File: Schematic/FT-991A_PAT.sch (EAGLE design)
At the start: 38 parts, among them Q1 PE4259, Q2 MC78L09, Q3 DG2001, Q5 NCP553, Q7 J310, Q8 BFR193F, X1 IF_IN, X2 SCP_OUT, X3 SDR_OUT

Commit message: Announcing: Revision U
Featuring:
* A properly matched BFR193F transistor, yielding 7 dB of gain,
  surpassing 2SC5086
* Larger pads for BFR193F
* Few routing improvements, larger wires
* Removed a via near the 3V regulator, didnt help a lot and was
  a short circuit risk.
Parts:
- C11, C12: value 330pF -> 1000pF
- C13: value 0.047µF -> 4.7 nF; device aarf:C-0805 -> aarf:C-1206
- C14: value 15pF -> 47pF
- L1: value 91nH -> 82nH
- R11: value 33kΩ -> 39kΩ
- R13: value 10Ω -> 27Ω
- R14: value 10Ω -> 47Ω
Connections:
- net BIAS renamed ST2OUT
- net IFIN renamed ST1IN
- net N$1 renamed ST2M2
- net N$3 renamed ST2M1
- net N$4 renamed ST2IN
- net N$5 renamed ST1M1
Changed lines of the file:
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@@
 <attribute name="PROJECT_INFO" value="Yaesu FT-991A Panadapter with Signal Control"/>
 <attribute name="PROJECT_NAME" value="FT-991A PAT &amp; SDR"/>
-<attribute name="REVISION_ID" value="T"/>
+<attribute name="REVISION_ID" value="U"/>
 </attributes>
 <variantdefs>
@@
 <part name="Q8" library="aarf" deviceset="BFR193F" device="" value="BFR193F"/>
 <part name="R7" library="aarf" deviceset="R-1206" device="" value="1kΩ"/>
-<part name="C11" library="aarf" deviceset="C-0805" device="" value="330pF"/>
+<part name="C11" library="aarf" deviceset="C-0805" device="" value="1000pF"/>
 <part name="GND11" library="supply1" deviceset="GNDA" device=""/>
 <part name="C2" library="aarf" deviceset="C-1206" device="" value="0.1µF"/>
 <part name="GND10" library="supply1" deviceset="GNDA" device=""/>
 <part name="C3" library="aarf" deviceset="C-1206" device="" value="0.1µF"/>
-<part name="R11" library="aarf" deviceset="R-1206" device="" value="33kΩ"/>
+<part name="R11" library="aarf" deviceset="R-1206" device="" value="39kΩ"/>
 <part name="GND19" library="supply1" deviceset="GNDA" device=""/>
 <part name="GND13" library="supply1" deviceset="GNDA" device=""/>
@@
 <part name="GND2" library="supply1" library_urn="urn:adsk.eagle:library:371" deviceset="GNDA" device=""/>
 <part name="L3" library="aarf" deviceset="FB-0805" device="" value="BLM21"/>
-<part name="C12" library="aarf" deviceset="C-0805" device="" value="330pF"/>
+<part name="C12" library="aarf" deviceset="C-0805" device="" value="1000pF"/>
 <part name="FRAME2" library="frames" library_urn="urn:adsk.eagle:library:229" deviceset="A3L-LOC" device=""/>
 <part name="GND5" library="supply1" library_urn="urn:adsk.eagle:library:371" deviceset="GNDA" device=""/>
@@
 <part name="GND7" library="supply1" deviceset="GNDA" device=""/>
 <part name="GND8" library="supply1" deviceset="GNDA" device=""/>
-<part name="R13" library="aarf" deviceset="R-1206" device="" value="10Ω"/>
+<part name="R13" library="aarf" deviceset="R-1206" device="" value="27Ω"/>
 <part name="R12" library="aarf" deviceset="R-1206" device="" value="100Ω"/>
-<part name="R14" library="aarf" deviceset="R-1206" device="" value="10Ω"/>
-<part name="C13" library="aarf" deviceset="C-0805" device="" value="0.047µF"/>
+<part name="R14" library="aarf" deviceset="R-1206" device="" value="47Ω"/>
+<part name="C13" library="aarf" deviceset="C-1206" device="" value="4.7 nF"/>
 <part name="GND9" library="supply1" deviceset="GNDA" device=""/>
-<part name="L1" library="aarf" deviceset="L-0805" device="" value="91nH">
+<part name="L1" library="aarf" deviceset="L-0805" device="" value="82nH">
 <spice>
 <pinmapping isusermap="yes" isdevicewide="yes">
@@
 <attribute name="SPICEPREFIX" value="L"/>
 </part>
-<part name="C14" library="aarf" deviceset="C-0805" device="" value="15pF"/>
+<part name="C14" library="aarf" deviceset="C-0805" device="" value="47pF"/>
 <part name="GND14" library="supply1" deviceset="GNDA" device=""/>
 </parts>
@@
 </busses>
 <nets>
-<net name="N$4" class="0">
+<net name="ST2IN" class="0">
 <segment>
 <pinref part="C11" gate="G$1" pin="2"/>
@@
 </segment>
 </net>
-<net name="N$5" class="0">
+<net name="ST1M1" class="0">
 <segment>
 <pinref part="R7" gate="G$1" pin="2"/>
@@
 </segment>
 </net>
-<net name="IFIN" class="0">
+<net name="ST1IN" class="0">
 <segment>
 <pinref part="Q1" gate="G$1" pin="RF2"/>
@@
 </segment>
 </net>
-<net name="BIAS" class="0">
+<net name="ST2OUT" class="0">
 <segment>
 <pinref part="R12" gate="G$1" pin="2"/>
@@
 </segment>
 </net>
-<net name="N$3" class="0">
+<net name="ST2M1" class="0">
 <segment>
 <pinref part="R14" gate="G$1" pin="2"/>
@@
 </segment>
 </net>
-<net name="N$1" class="0">
+<net name="ST2M2" class="0">
 <segment>
 <pinref part="C12" gate="G$1" pin="2"/>

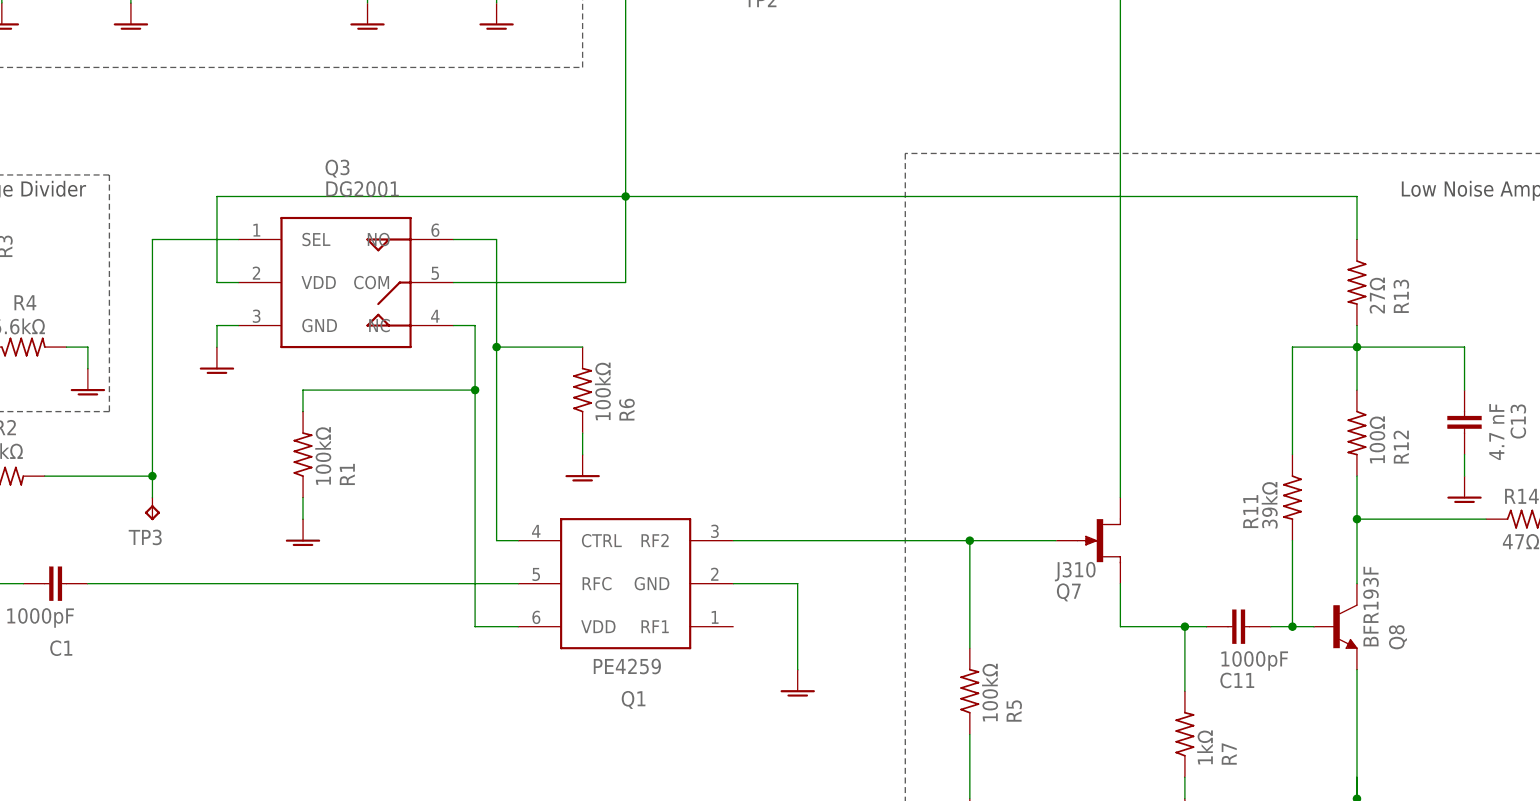
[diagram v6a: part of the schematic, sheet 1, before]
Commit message: Updating Schematic and Board
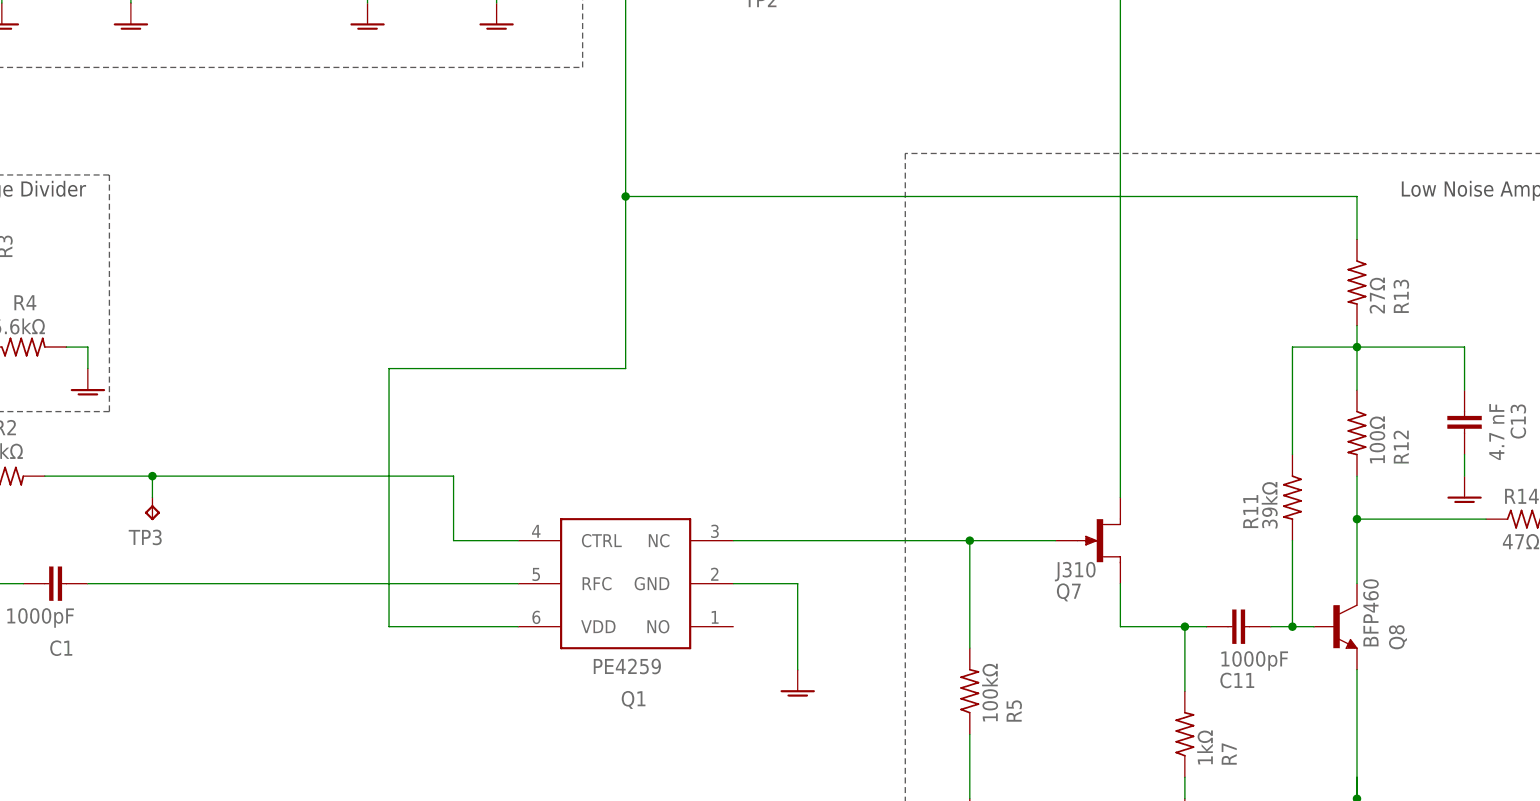
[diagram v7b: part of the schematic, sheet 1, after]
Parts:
- removed Q3: DG2001, aarf:NLAS4599
- removed R1, R6: 100kΩ, aarf:R-1206
- Q8: value BFR193F -> BFP460; device aarf:BFR193F -> aarf:BFP460
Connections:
- removed net NC: Q1.VDD, Q3.NC, R1.2
- removed net NO: Q1.CTRL, Q3.NO, R6.2
- net 3V: now also Q1.VDD; no longer Q3.COM, Q3.VDD
- net GNDA: no longer Q3.GND, R1.1, R6.1
- net N$7: now also Q1.CTRL; no longer Q3.SEL
- net ST1IN: now also Q1.NC; no longer Q1.RF2
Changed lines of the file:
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@@
 <parts>
 <part name="R5" library="aarf" deviceset="R-1206" device="" value="100kΩ"/>
-<part name="Q8" library="aarf" deviceset="BFR193F" device="" value="BFR193F"/>
+<part name="Q8" library="aarf" deviceset="BFP460" device="" value="BFP460"/>
 <part name="R7" library="aarf" deviceset="R-1206" device="" value="1kΩ"/>
 <part name="C11" library="aarf" deviceset="C-0805" device="" value="1000pF"/>
@@
 <part name="GND" library="wirepad" library_urn="urn:adsk.eagle:library:412" deviceset="WIREPAD" device="SMD1,27-254" package3d_urn="urn:adsk.eagle:package:30839/1" value="GND"/>
 <part name="GND3" library="supply1" library_urn="urn:adsk.eagle:library:371" deviceset="GNDA" device=""/>
-<part name="Q3" library="aarf" deviceset="NLAS4599" device="" value="DG2001"/>
-<part name="R1" library="aarf" deviceset="R-1206" device="" value="100kΩ"/>
-<part name="GND6" library="supply1" deviceset="GNDA" device=""/>
-<part name="R6" library="aarf" deviceset="R-1206" device="" value="100kΩ"/>
-<part name="GND7" library="supply1" deviceset="GNDA" device=""/>
-<part name="GND8" library="supply1" deviceset="GNDA" device=""/>
 <part name="R13" library="aarf" deviceset="R-1206" device="" value="27Ω"/>
 <part name="R12" library="aarf" deviceset="R-1206" device="" value="100Ω"/>
@@
 </instance>
 <instance part="GND3" gate="1" x="38.1" y="162.56" smashed="yes"/>
-<instance part="Q3" gate="G$1" x="142.24" y="134.62" smashed="yes">
-<attribute name="NAME" x="139.7" y="147.32" size="1.778" layer="95"/>
-<attribute name="VALUE" x="139.7" y="144.78" size="1.778" layer="96"/>
-</instance>
-<instance part="R1" gate="G$1" x="137.16" y="114.3" smashed="yes" rot="R90">
-<attribute name="NAME" x="143.2814" y="110.49" size="1.778" layer="95" rot="R90"/>
-<attribute name="VALUE" x="140.462" y="110.49" size="1.778" layer="96" rot="R90"/>
-</instance>
-<instance part="GND6" gate="1" x="137.16" y="104.14" smashed="yes"/>
-<instance part="R6" gate="G$1" x="170.18" y="121.92" smashed="yes" rot="R90">
-<attribute name="NAME" x="176.3014" y="118.11" size="1.778" layer="95" rot="R90"/>
-<attribute name="VALUE" x="173.482" y="118.11" size="1.778" layer="96" rot="R90"/>
-</instance>
-<instance part="GND7" gate="1" x="170.18" y="111.76" smashed="yes"/>
-<instance part="GND8" gate="1" x="127" y="124.46" smashed="yes"/>
 <instance part="R13" gate="G$1" x="261.62" y="134.62" smashed="yes" rot="R270">
 <attribute name="NAME" x="267.7414" y="130.81" size="1.778" layer="95" rot="R90"/>
@@
 </segment>
 <segment>
-<pinref part="R1" gate="G$1" pin="1"/>
-<pinref part="GND6" gate="1" pin="GNDA"/>
-<wire x1="137.16" y1="109.22" x2="137.16" y2="106.68" width="0.1524" layer="91"/>
-</segment>
-<segment>
-<pinref part="R6" gate="G$1" pin="1"/>
-<pinref part="GND7" gate="1" pin="GNDA"/>
-<wire x1="170.18" y1="116.84" x2="170.18" y2="114.3" width="0.1524" layer="91"/>
-</segment>
-<segment>
-<pinref part="Q3" gate="G$1" pin="GND"/>
-<pinref part="GND8" gate="1" pin="GNDA"/>
-<wire x1="129.54" y1="129.54" x2="127" y2="129.54" width="0.1524" layer="91"/>
-<wire x1="127" y1="129.54" x2="127" y2="127" width="0.1524" layer="91"/>
-</segment>
-<segment>
 <pinref part="C13" gate="G$1" pin="2"/>
 <pinref part="GND9" gate="1" pin="GNDA"/>
@@
 <net name="ST1IN" class="0">
 <segment>
-<pinref part="Q1" gate="G$1" pin="RF2"/>
+<pinref part="Q1" gate="G$1" pin="NC"/>
 <wire x1="187.96" y1="104.14" x2="215.9" y2="104.14" width="0.1524" layer="91"/>
 <pinref part="R5" gate="G$1" pin="2"/>
@@
 <pinref part="TP3" gate="G$1" pin="TP"/>
 <wire x1="119.38" y1="109.22" x2="119.38" y2="111.76" width="0.1524" layer="91"/>
-<pinref part="Q3" gate="G$1" pin="SEL"/>
-<wire x1="119.38" y1="111.76" x2="119.38" y2="139.7" width="0.1524" layer="91"/>
-<wire x1="119.38" y1="139.7" x2="129.54" y2="139.7" width="0.1524" layer="91"/>
+<wire x1="119.38" y1="111.76" x2="154.94" y2="111.76" width="0.1524" layer="91"/>
 <junction x="119.38" y="111.76"/>
+<wire x1="154.94" y1="111.76" x2="154.94" y2="104.14" width="0.1524" layer="91"/>
+<pinref part="Q1" gate="G$1" pin="CTRL"/>
+<wire x1="154.94" y1="104.14" x2="162.56" y2="104.14" width="0.1524" layer="91"/>
 </segment>
 </net>
@@
 <wire x1="160.02" y1="185.42" x2="160.02" y2="177.8" width="0.1524" layer="91"/>
 <junction x="160.02" y="185.42"/>
-<pinref part="Q3" gate="G$1" pin="VDD"/>
-<wire x1="129.54" y1="134.62" x2="127" y2="134.62" width="0.1524" layer="91"/>
-<wire x1="127" y1="134.62" x2="127" y2="144.78" width="0.1524" layer="91"/>
-<wire x1="127" y1="144.78" x2="175.26" y2="144.78" width="0.1524" layer="91"/>
 <junction x="175.26" y="144.78"/>
-<pinref part="Q3" gate="G$1" pin="COM"/>
-<wire x1="175.26" y1="144.78" x2="175.26" y2="134.62" width="0.1524" layer="91"/>
-<wire x1="175.26" y1="134.62" x2="154.94" y2="134.62" width="0.1524" layer="91"/>
 <pinref part="R13" gate="G$1" pin="1"/>
+<wire x1="175.26" y1="144.78" x2="175.26" y2="124.46" width="0.1524" layer="91"/>
+<wire x1="175.26" y1="124.46" x2="147.32" y2="124.46" width="0.1524" layer="91"/>
+<wire x1="147.32" y1="124.46" x2="147.32" y2="93.98" width="0.1524" layer="91"/>
+<pinref part="Q1" gate="G$1" pin="VDD"/>
+<wire x1="147.32" y1="93.98" x2="162.56" y2="93.98" width="0.1524" layer="91"/>
 </segment>
 </net>
@@
 </segment>
 </net>
-<net name="NC" class="0">
-<segment>
-<pinref part="R1" gate="G$1" pin="2"/>
-<wire x1="137.16" y1="121.92" x2="137.16" y2="119.38" width="0.1524" layer="91"/>
-<pinref part="Q1" gate="G$1" pin="VDD"/>
-<wire x1="162.56" y1="93.98" x2="157.48" y2="93.98" width="0.1524" layer="91"/>
-<wire x1="157.48" y1="93.98" x2="157.48" y2="121.92" width="0.1524" layer="91"/>
-<wire x1="137.16" y1="121.92" x2="157.48" y2="121.92" width="0.1524" layer="91"/>
-<pinref part="Q3" gate="G$1" pin="NC"/>
-<wire x1="154.94" y1="129.54" x2="157.48" y2="129.54" width="0.1524" layer="91"/>
-<wire x1="157.48" y1="129.54" x2="157.48" y2="121.92" width="0.1524" layer="91"/>
-<junction x="157.48" y="121.92"/>
-</segment>
-</net>
-<net name="NO" class="0">
-<segment>
-<pinref part="Q1" gate="G$1" pin="CTRL"/>
-<wire x1="160.02" y1="127" x2="160.02" y2="104.14" width="0.1524" layer="91"/>
-<wire x1="160.02" y1="104.14" x2="162.56" y2="104.14" width="0.1524" layer="91"/>
-<pinref part="R6" gate="G$1" pin="2"/>
-<wire x1="160.02" y1="127" x2="170.18" y2="127" width="0.1524" layer="91"/>
-<junction x="160.02" y="127"/>
-<wire x1="160.02" y1="127" x2="160.02" y2="139.7" width="0.1524" layer="91"/>
-<pinref part="Q3" gate="G$1" pin="NO"/>
-<wire x1="160.02" y1="139.7" x2="154.94" y2="139.7" width="0.1524" layer="91"/>
-</segment>
-</net>

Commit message: Revision V: Improvements
* Improved BFP460 and NCP553 footprint
* Some routing  and CPW improvements
* Rebasing the library to the latest
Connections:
- net N$18 renamed TX9
- net N$7 renamed SW_FLIP
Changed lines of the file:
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@@
 </segment>
 </net>
-<net name="N$18" class="0">
+<net name="TX9" class="0">
 <segment>
 <pinref part="PAD3" gate="G$1" pin="P"/>
@@
 </segment>
 </net>
-<net name="N$7" class="0">
+<net name="SW_FLIP" class="0">
 <segment>
 <pinref part="R2" gate="G$1" pin="2"/>
